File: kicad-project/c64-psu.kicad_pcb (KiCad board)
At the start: 2 copper layers, 116 x 74 mm, 50 parts, among them J1 Conn_01x01, J2 Conn_01x01, J3 Conn_01x01, J4 Conn_01x01, J5 Conn_01x01, J6 Conn_01x01, Q1 N-MOS, U1 LMR33630A, U2 MAX6399

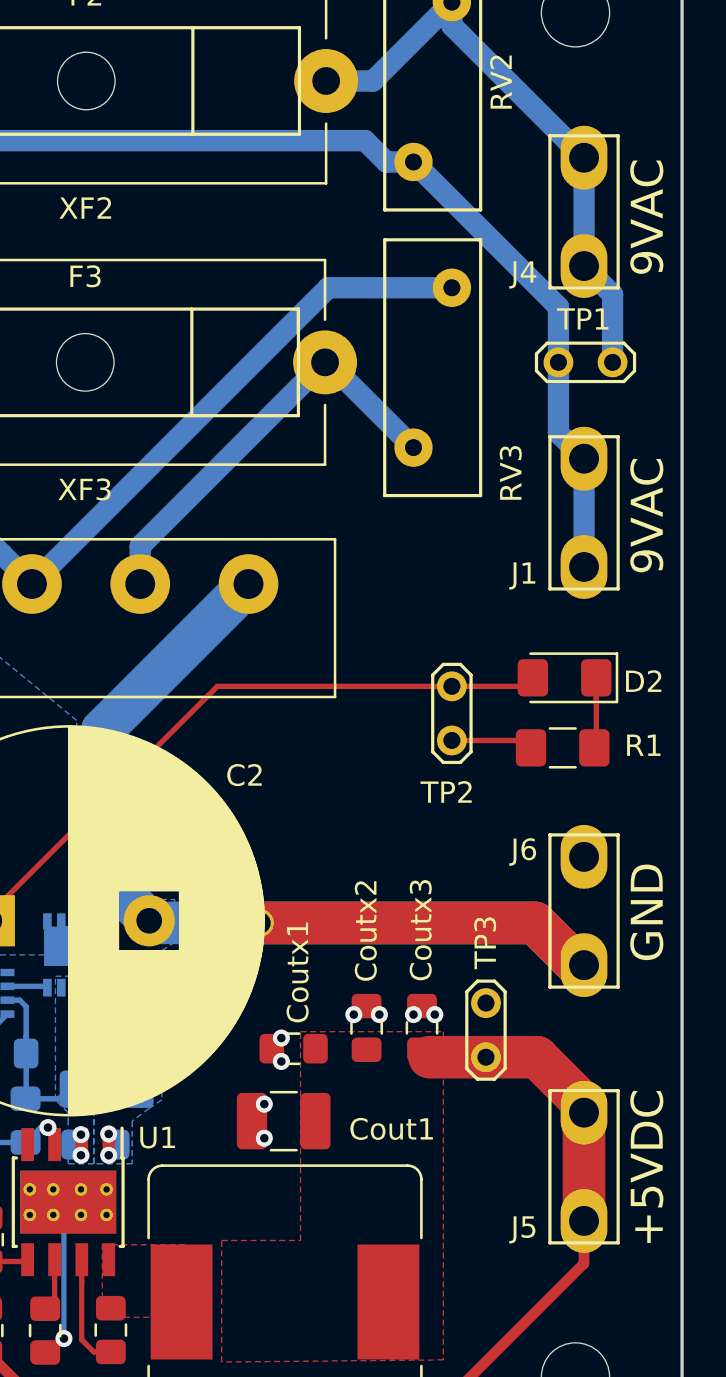
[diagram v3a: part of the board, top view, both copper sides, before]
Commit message: fixed bug: copper fill under spade connectors to prevent ground plane shorts
gerbers + bom redone
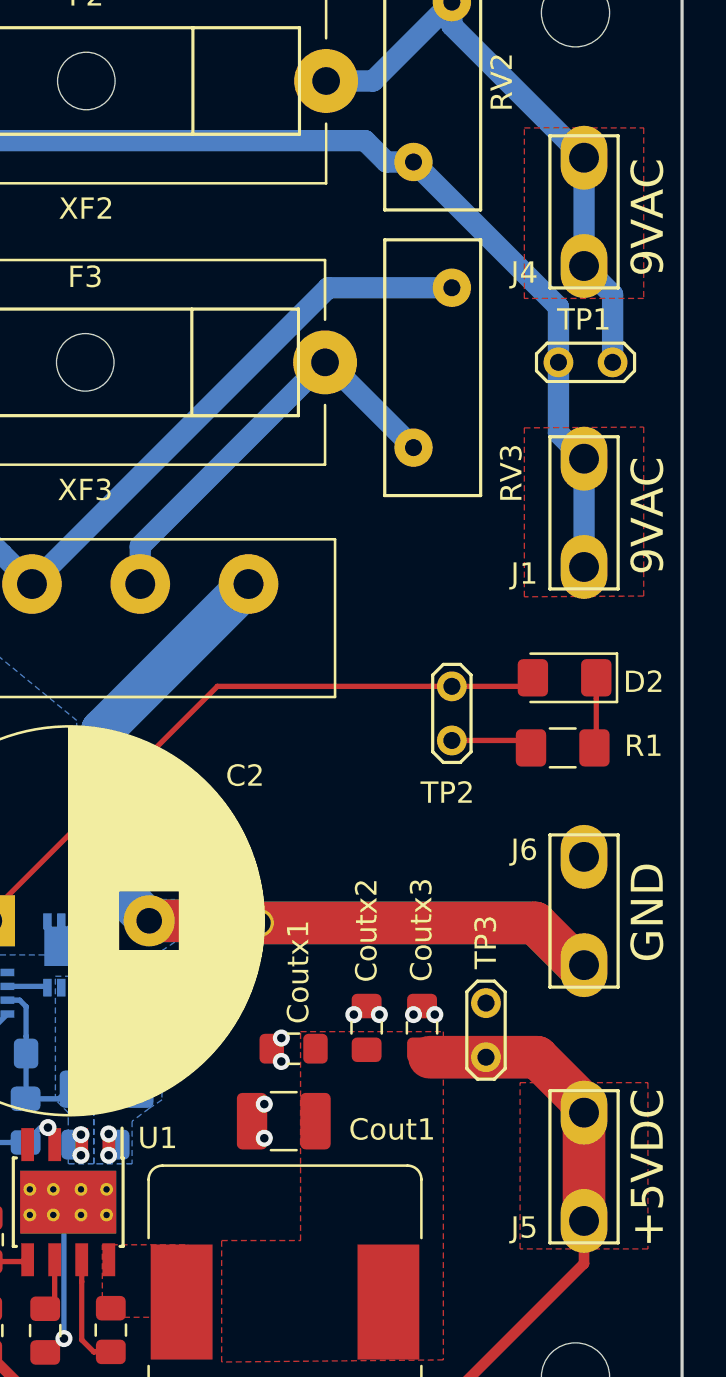
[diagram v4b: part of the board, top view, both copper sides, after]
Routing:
- net GNDPWR: track 22.2 -> 24.8 mm
- added copper zone on F.Cu, net /SEC1B
- added copper zone on F.Cu, net Net-(J4-Pad1)
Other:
- board text added: "v2019.1"
- board text removed: "v2018.2"
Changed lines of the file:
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@@
     (thickness 1.6)
     (drawings 11)
-    (tracks 173)
+    (tracks 175)
     (zones 0)
     (modules 50)
@@
     (35 F.Paste user hide)
     (36 B.SilkS user)
-    (37 F.SilkS user)
+    (37 F.SilkS user hide)
     (38 B.Mask user)
     (39 F.Mask user)
@@
       (xy -10.075333 -31.157333)) (layer B.SilkS) (width 0.01))
   )
-  (gr_text v2018.2 (at 108.4 127.8) (layer B.SilkS)
+  (gr_text v2019.1 (at 108.4 127.8) (layer B.SilkS)
     (effects (font (size 1.5 1.5) (thickness 0.3)) (justify mirror))
   )
@@
   (via (at 178.1 119.6) (size 0.8) (drill 0.4) (layers F.Cu B.Cu) (net 20))
   (via (at 178.1 120.6) (size 0.8) (drill 0.4) (layers F.Cu B.Cu) (net 20))
-  (segment (start 180.1 109.7) (end 180 109.6) (width 2) (layer B.Cu) (net 20))
-  (segment (start 182.6 109.7) (end 180.1 109.7) (width 2) (layer B.Cu) (net 20))
   (segment (start 177.8 100.66) (end 184.66 93.8) (width 2) (layer B.Cu) (net 20))
   (segment (start 177.8 107.4) (end 177.8 100.66) (width 2) (layer B.Cu) (net 20))
   (segment (start 180 109.6) (end 177.8 107.4) (width 2) (layer B.Cu) (net 20))
+  (segment (start 182.5 109.6) (end 182.6 109.7) (width 2) (layer B.Cu) (net 20))
+  (segment (start 180 109.6) (end 182.5 109.6) (width 2) (layer B.Cu) (net 20))
+  (segment (start 182.5 109.6) (end 182.6 109.7) (width 2) (layer F.Cu) (net 20))
+  (segment (start 180 109.6) (end 182.5 109.6) (width 2) (layer F.Cu) (net 20))
   (segment (start 175.165 112.675) (end 175.225 112.735) (width 0.25) (layer B.Cu) (net 21))
   (segment (start 173.35 112.675) (end 175.165 112.675) (width 0.25) (layer B.Cu) (net 21))
@@
       )
     )
+  )
+  (zone (net 22) (net_name "Net-(J4-Pad1)") (layer F.Cu) (hatch edge 0.508)
+    (priority 5)
+    (connect_pads yes (clearance 0.254))
+    (min_thickness 0.254)
+    (fill yes (arc_segments 16) (thermal_gap 0.508) (thermal_bridge_width 0.508) (smoothing chamfer) (radius 1))
+    (polygon
+      (pts
+        (xy 197.6 72.4) (xy 203.2 72.4) (xy 203.2 80.4) (xy 197.6 80.4)
+      )
+    )
+  )
+  (zone (net 6) (net_name /SEC1B) (layer F.Cu) (hatch edge 0.508)
+    (priority 5)
+    (connect_pads yes (clearance 0.254))
+    (min_thickness 0.254)
+    (fill yes (arc_segments 16) (thermal_gap 0.508) (thermal_bridge_width 0.508) (smoothing chamfer) (radius 1))
+    (polygon
+      (pts
+        (xy 197.6 86.474054) (xy 203.2 86.437027) (xy 203.2 94.362974) (xy 197.6 94.400001)
+      )
+    )
+  )
+  (zone (net 8) (net_name /VOUT) (layer F.Cu) (hatch edge 0.508)
+    (priority 5)
+    (connect_pads yes (clearance 0.254))
+    (min_thickness 0.254)
+    (fill yes (arc_segments 16) (thermal_gap 0.508) (thermal_bridge_width 0.508) (smoothing chamfer) (radius 1))
+    (polygon
+      (pts
+        (xy 197.4 117.194204) (xy 203.4 117.194204) (xy 203.4 124.994204) (xy 197.4 124.994204)
+      )
+    )
